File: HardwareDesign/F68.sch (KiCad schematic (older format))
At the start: 2 parts, among them J001 Conn_02x40_Counter_Clockwise

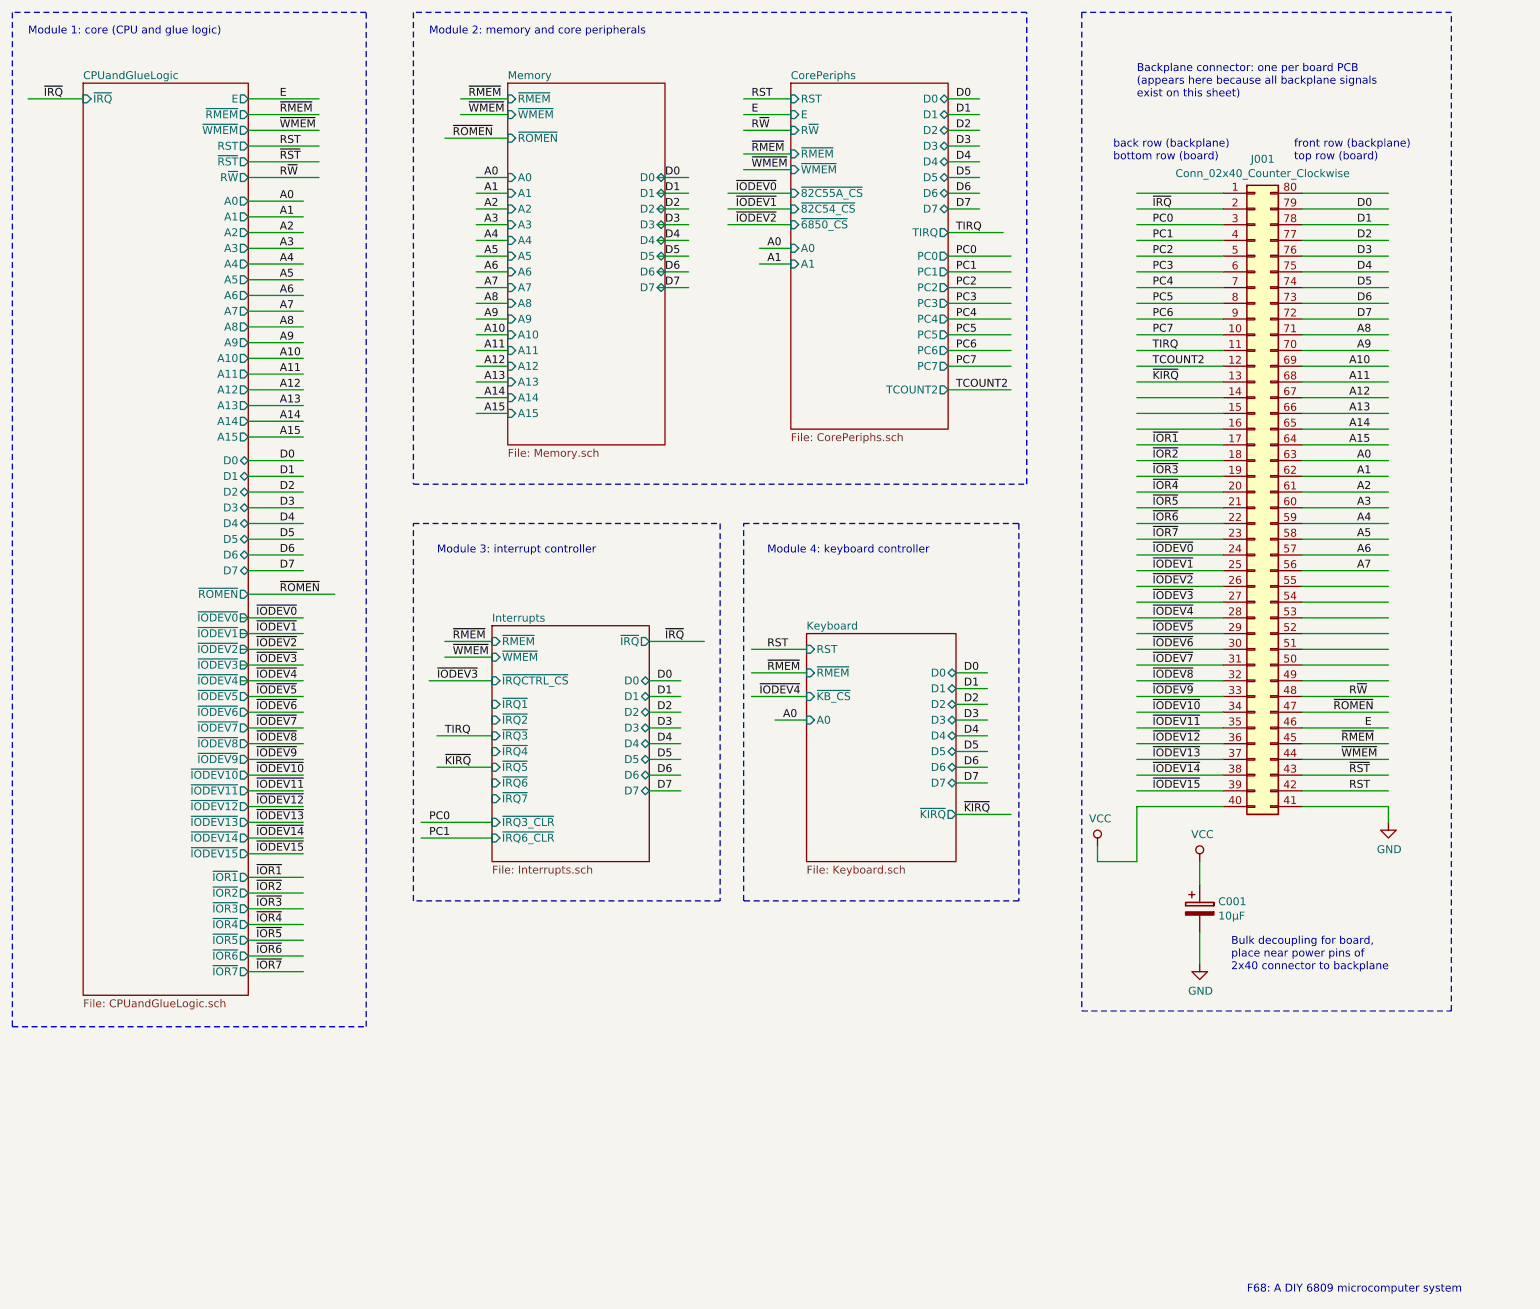
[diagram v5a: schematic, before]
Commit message: changes to backplane signals
Route all IRQ signals on backplane.

Only route -IOR1..-IOR3 on backplane.

Move TCOUNT2 to after IRQ signals.
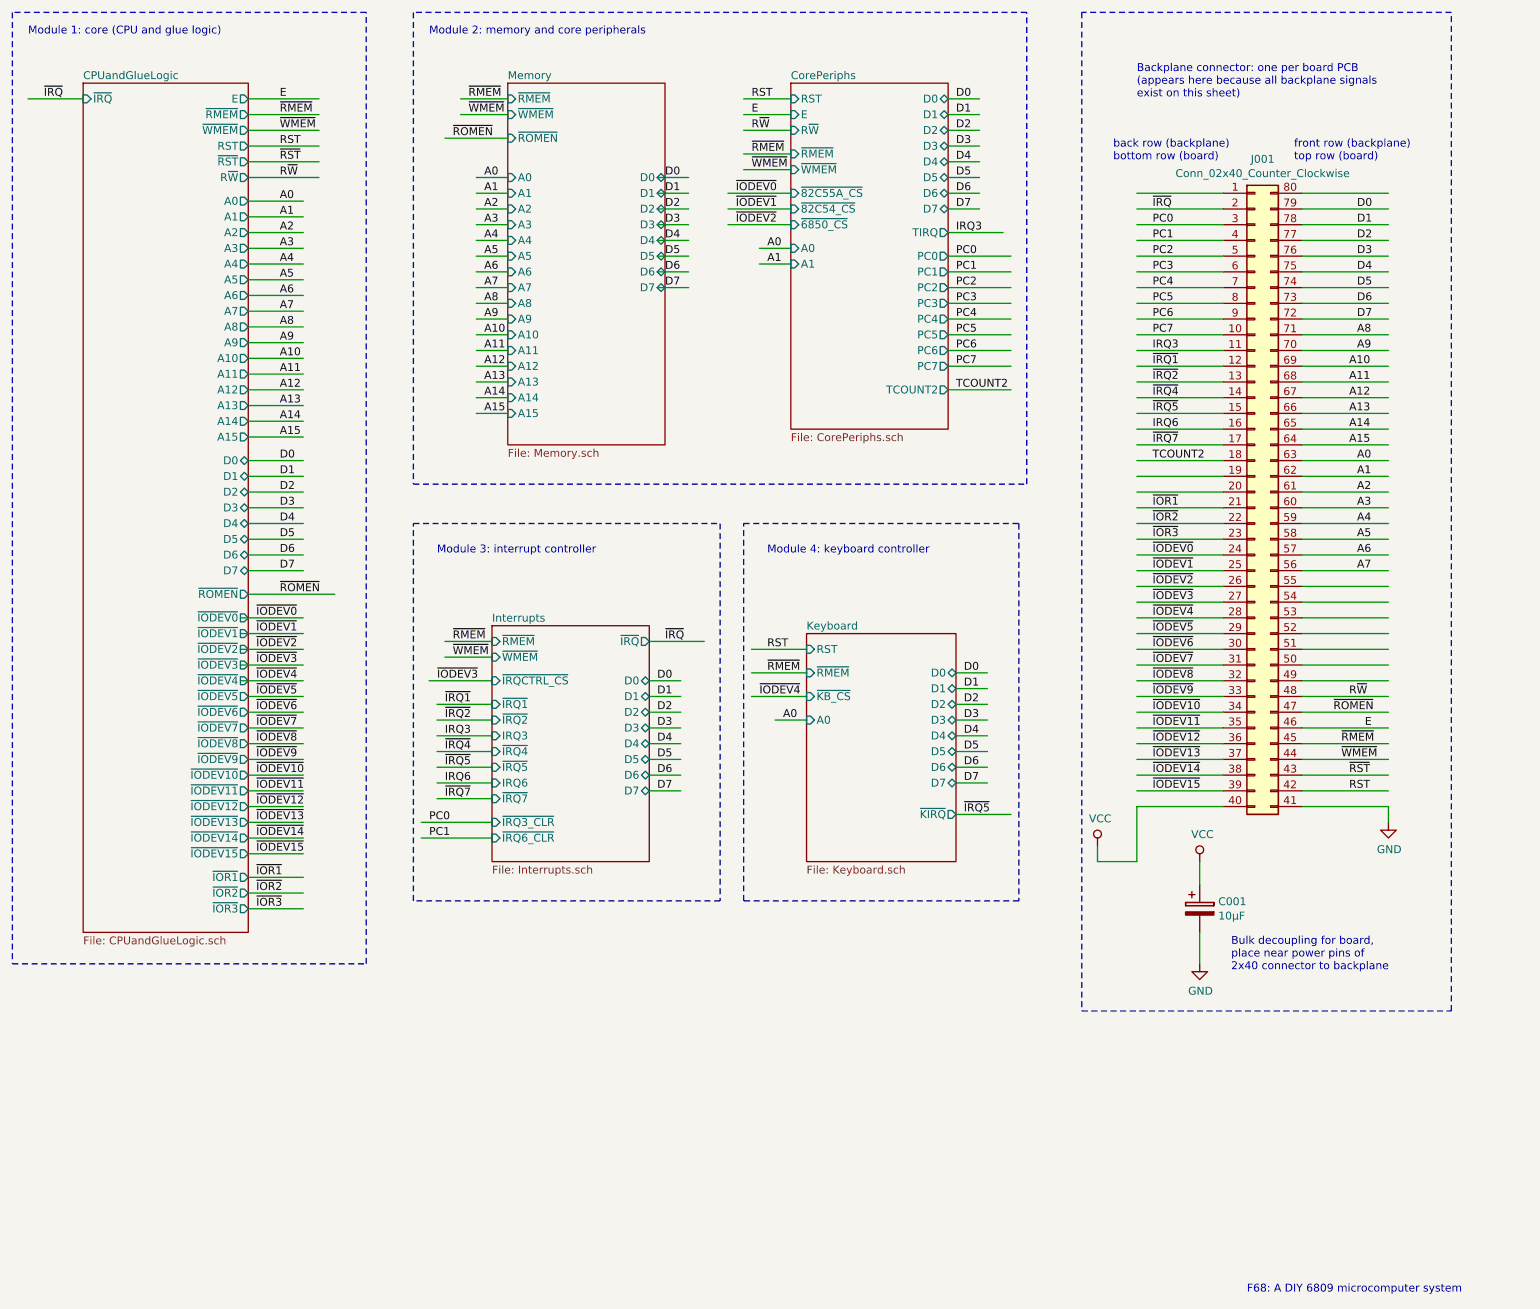
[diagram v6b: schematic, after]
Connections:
- net labels added: IRQ3, IRQ6, ~IRQ1~, ~IRQ2~, ~IRQ4~, ~IRQ5~, ~IRQ7~
- net labels removed: TIRQ, ~IOR4~, ~IOR5~, ~IOR6~, ~IOR7~, ~KIRQ~
- wire segments 225 -> 226
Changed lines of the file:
@@
 F68: A DIY 6809 microcomputer system
 $Sheet
-S 2200 1700 1050 5800
+S 2200 1700 1050 5400
 U 5CFA6AAA
 F0 "CPUandGlueLogic" 50
@@
 F51 "~IOR2~" O R 3250 6850 50
 F52 "~IOR3~" O R 3250 6950 50
-F53 "~IOR4~" O R 3250 7050 50
-F54 "~IOR5~" O R 3250 7150 50
-F55 "~IOR6~" O R 3250 7250 50
-F56 "~IOR7~" O R 3250 7350 50
 $EndSheet
 $Sheet
@@
 ~IODEV2
 Wire Notes Line
-	1750 1250 1750 7700
-Wire Notes Line
-	1750 7700 4000 7700
-Wire Notes Line
-	4000 7700 4000 1250
+	1750 1250 1750 7300
+Wire Notes Line
+	1750 7300 4000 7300
+Wire Notes Line
+	4000 7300 4000 1250
 Wire Notes Line
 	4000 1250 1750 1250
@@
 F5 "~IRQ5" I L 4800 6050 50
 F6 "~IRQ7" I L 4800 6250 50
-F7 "~IRQ3" I L 4800 5850 50
-F8 "~IRQ6" I L 4800 6150 50
-F9 "~IRQ" O R 5800 5250 50
-F10 "~RMEM" I L 4800 5250 50
-F11 "~IRQCTRL_CS" I L 4800 5500 50
-F12 "~IRQ3_CLR" I L 4800 6400 50
-F13 "~IRQ6_CLR" I L 4800 6500 50
-F14 "D0" B R 5800 5500 50
-F15 "D1" B R 5800 5600 50
-F16 "D2" B R 5800 5700 50
-F17 "D3" B R 5800 5800 50
-F18 "D4" B R 5800 5900 50
-F19 "D5" B R 5800 6000 50
-F20 "D6" B R 5800 6100 50
-F21 "D7" B R 5800 6200 50
-F22 "~WMEM" I L 4800 5350 50
+F7 "~IRQ" O R 5800 5250 50
+F8 "~RMEM" I L 4800 5250 50
+F9 "~IRQCTRL_CS" I L 4800 5500 50
+F10 "~IRQ3_CLR" I L 4800 6400 50
+F11 "~IRQ6_CLR" I L 4800 6500 50
+F12 "D0" B R 5800 5500 50
+F13 "D1" B R 5800 5600 50
+F14 "D2" B R 5800 5700 50
+F15 "D3" B R 5800 5800 50
+F16 "D4" B R 5800 5900 50
+F17 "D5" B R 5800 6000 50
+F18 "D6" B R 5800 6100 50
+F19 "D7" B R 5800 6200 50
+F20 "~WMEM" I L 4800 5350 50
+F21 "IRQ3" I L 4800 5850 50
+F22 "IRQ6" I L 4800 6150 50
 $EndSheet
 Wire Notes Line
@@
 	7700 2650 8050 2650
 Text Label 7750 2650 0    50   ~ 0
-TIRQ
+IRQ3
 Wire Wire Line
 	4450 5850 4800 5850
 Text Label 4500 5850 0    50   ~ 0
-TIRQ
+IRQ3
 Wire Wire Line
 	7700 2800 8100 2800
@@
 	7750 6350 8100 6350
 Text Label 7800 6350 0    50   ~ 0
-~KIRQ~
+~IRQ5~
 Wire Wire Line
 	4450 6050 4800 6050
 Text Label 4500 6050 0    50   ~ 0
-~KIRQ~
+~IRQ5~
 Wire Wire Line
 	7700 3650 8100 3650
@@
 	8900 3900 9450 3900
 Wire Wire Line
+	9950 4900 10500 4900
+Wire Wire Line
+	9950 5000 10500 5000
+Wire Wire Line
+	9950 5100 10500 5100
+Wire Wire Line
+	9950 5200 10500 5200
+Wire Wire Line
+	9950 5300 10500 5300
+Wire Wire Line
+	9950 5400 10500 5400
+Wire Wire Line
+	9950 5500 10500 5500
+Wire Wire Line
+	8900 4700 9450 4700
+Wire Wire Line
+	8900 4800 9450 4800
+Wire Wire Line
+	8900 4900 9450 4900
+Wire Wire Line
+	8900 5000 9450 5000
+Wire Wire Line
+	8900 5100 9450 5100
+Wire Wire Line
+	8900 5200 9450 5200
+Wire Wire Line
+	8900 5300 9450 5300
+Wire Wire Line
+	8900 5400 9450 5400
+Wire Wire Line
+	8900 5500 9450 5500
+Wire Wire Line
+	8900 5600 9450 5600
+Wire Wire Line
+	8900 5700 9450 5700
+Wire Wire Line
+	8900 5800 9450 5800
+Wire Wire Line
+	8900 5900 9450 5900
+Wire Wire Line
+	8900 6000 9450 6000
+Wire Wire Line
+	8900 6100 9450 6100
+Wire Wire Line
+	8900 6200 9450 6200
+Wire Wire Line
+	8900 6300 9450 6300
+Wire Wire Line
+	9950 2400 10500 2400
+Wire Wire Line
+	9950 2500 10500 2500
+Wire Wire Line
+	9950 2600 10500 2600
+Wire Wire Line
+	9950 2700 10500 2700
+Wire Wire Line
+	9950 2800 10500 2800
+Wire Wire Line
+	9950 2900 10500 2900
+Wire Wire Line
+	9950 3000 10500 3000
+Wire Wire Line
+	9950 3100 10500 3100
+Wire Wire Line
+	9950 3200 10500 3200
+Wire Wire Line
+	9950 3300 10500 3300
+Wire Wire Line
+	9950 3400 10500 3400
+Wire Wire Line
+	9950 3500 10500 3500
+Wire Wire Line
+	9950 3600 10500 3600
+Wire Wire Line
+	9950 3700 10500 3700
+Wire Wire Line
+	9950 3800 10500 3800
+Wire Wire Line
+	9950 3900 10500 3900
+Wire Wire Line
+	9950 4000 10500 4000
+Wire Wire Line
+	9950 4100 10500 4100
+Wire Wire Line
+	9950 4200 10500 4200
+Wire Wire Line
+	9950 4300 10500 4300
+Wire Wire Line
+	9950 4400 10500 4400
+Wire Wire Line
+	9950 4500 10500 4500
+Wire Wire Line
+	9950 4600 10500 4600
+Wire Wire Line
+	9950 4700 10500 4700
+Wire Wire Line
+	9950 4800 10500 4800
+Wire Wire Line
 	8900 4000 9450 4000
 Wire Wire Line
@@
 Wire Wire Line
 	8900 4600 9450 4600
-Wire Wire Line
-	8900 4700 9450 4700
-Wire Wire Line
-	8900 4800 9450 4800
-Wire Wire Line
-	8900 4900 9450 4900
-Wire Wire Line
-	8900 5000 9450 5000
-Wire Wire Line
-	8900 5100 9450 5100
-Wire Wire Line
-	8900 5200 9450 5200
-Wire Wire Line
-	8900 5300 9450 5300
-Wire Wire Line
-	8900 5400 9450 5400
-Wire Wire Line
-	8900 5500 9450 5500
-Wire Wire Line
-	8900 5600 9450 5600
-Wire Wire Line
-	8900 5700 9450 5700
-Wire Wire Line
-	8900 5800 9450 5800
-Wire Wire Line
-	8900 5900 9450 5900
-Wire Wire Line
-	8900 6000 9450 6000
-Wire Wire Line
-	8900 6100 9450 6100
-Wire Wire Line
-	8900 6200 9450 6200
-Wire Wire Line
-	8900 6300 9450 6300
-Wire Wire Line
-	9950 2400 10500 2400
-Wire Wire Line
-	9950 2500 10500 2500
-Wire Wire Line
-	9950 2600 10500 2600
-Wire Wire Line
-	9950 2700 10500 2700
-Wire Wire Line
-	9950 2800 10500 2800
-Wire Wire Line
-	9950 2900 10500 2900
-Wire Wire Line
-	9950 3000 10500 3000
-Wire Wire Line
-	9950 3100 10500 3100
-Wire Wire Line
-	9950 3200 10500 3200
-Wire Wire Line
-	9950 3300 10500 3300
-Wire Wire Line
-	9950 3400 10500 3400
-Wire Wire Line
-	9950 3500 10500 3500
-Wire Wire Line
-	9950 3600 10500 3600
-Wire Wire Line
-	9950 3700 10500 3700
-Wire Wire Line
-	9950 3800 10500 3800
-Wire Wire Line
-	9950 3900 10500 3900
-Wire Wire Line
-	9950 4000 10500 4000
-Wire Wire Line
-	9950 4100 10500 4100
-Wire Wire Line
-	9950 4200 10500 4200
-Wire Wire Line
-	9950 4300 10500 4300
-Wire Wire Line
-	9950 4400 10500 4400
-Wire Wire Line
-	9950 4500 10500 4500
-Wire Wire Line
-	9950 4600 10500 4600
-Wire Wire Line
-	9950 4700 10500 4700
-Wire Wire Line
-	9950 4800 10500 4800
-Wire Wire Line
-	9950 4900 10500 4900
-Wire Wire Line
-	9950 5000 10500 5000
-Wire Wire Line
-	9950 5100 10500 5100
-Wire Wire Line
-	9950 5200 10500 5200
-Wire Wire Line
-	9950 5300 10500 5300
-Wire Wire Line
-	9950 5400 10500 5400
-Wire Wire Line
-	9950 5500 10500 5500
 Wire Wire Line
 	9950 5600 10500 5600
@@
 PC7
 Text Label 9000 3400 0    50   ~ 0
-TIRQ
+IRQ3
 Wire Wire Line
 	8650 6650 8650 6550
@@
 Text Notes 9900 2200 0    50   ~ 0
 front row (backplane)\ntop row (board)
-Text Label 9000 4000 0    50   ~ 0
+Text Label 9000 4400 0    50   ~ 0
 ~IOR1~
+Text Label 9000 4500 0    50   ~ 0
+~IOR2~
+Text Label 9000 4600 0    50   ~ 0
+~IOR3~
 Text Label 9000 4100 0    50   ~ 0
-~IOR2~
-Text Label 9000 4200 0    50   ~ 0
-~IOR3~
-Text Label 9000 4300 0    50   ~ 0
-~IOR4~
-Text Label 9000 4400 0    50   ~ 0
-~IOR5~
-Text Label 9000 4500 0    50   ~ 0
-~IOR6~
-Text Label 9000 4600 0    50   ~ 0
-~IOR7~
-Text Label 9000 3500 0    50   ~ 0
 TCOUNT2
 Text Notes 8900 1800 0    50   ~ 0
@@
 Wire Wire Line
 	3250 6950 3600 6950
-Wire Wire Line
-	3250 7050 3600 7050
-Wire Wire Line
-	3250 7150 3600 7150
-Wire Wire Line
-	3250 7250 3600 7250
-Wire Wire Line
-	3250 7350 3600 7350
 Text Label 3300 6750 0    50   ~ 0
 ~IOR1~
@@
 Text Label 3300 6950 0    50   ~ 0
 ~IOR3~
-Text Label 3300 7050 0    50   ~ 0
-~IOR4~
-Text Label 3300 7150 0    50   ~ 0
-~IOR5~
-Text Label 3300 7250 0    50   ~ 0
-~IOR6~
-Text Label 3300 7350 0    50   ~ 0
-~IOR7~
-Text Label 9000 3600 0    50   ~ 0
-~KIRQ~
 Wire Notes Line
 	8550 1250 8550 7600
@@
 Text Notes 9500 7350 0    50   ~ 0
 Bulk decoupling for board,\nplace near power pins of\n2x40 connector to backplane
+Text Label 9000 3800 0    50   ~ 0
+~IRQ5~
+Text Label 9000 3500 0    50   ~ 0
+~IRQ1~
+Text Label 9000 3600 0    50   ~ 0
+~IRQ2~
+Text Label 9000 3700 0    50   ~ 0
+~IRQ4~
+Text Label 9000 3900 0    50   ~ 0
+IRQ6
+Text Label 9000 4000 0    50   ~ 0
+~IRQ7~
+Wire Wire Line
+	4450 5650 4800 5650
+Wire Wire Line
+	4450 5750 4800 5750
+Text Label 4500 5650 0    50   ~ 0
+~IRQ1~
+Text Label 4500 5750 0    50   ~ 0
+~IRQ2~
+Wire Wire Line
+	4450 5950 4800 5950
+Text Label 4500 5950 0    50   ~ 0
+~IRQ4~
+Wire Wire Line
+	4450 6150 4800 6150
+Wire Wire Line
+	4450 6250 4800 6250
+Text Label 4500 6150 0    50   ~ 0
+IRQ6
+Text Label 4500 6250 0    50   ~ 0
+~IRQ7~
 $EndSCHEMATC

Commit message: assigned component footprints
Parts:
- C001: footprint (none) -> Capacitor_THT:CP_Radial_D6.3mm_P2.50mm
- J001: footprint (none) -> Connector_PinHeader_2.54mm:PinHeader_2x40_P2.54mm_Vertical
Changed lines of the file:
@@
 F 0 "J001" H 9700 6417 50  0000 C CNN
 F 1 "Conn_02x40_Counter_Clockwise" H 9700 6326 50  0000 C CNN
-F 2 "" H 9650 4300 50  0001 C CNN
+F 2 "Connector_PinHeader_2.54mm:PinHeader_2x40_P2.54mm_Vertical" H 9650 4300 50  0001 C CNN
 F 3 "~" H 9650 4300 50  0001 C CNN
 	1    9650 4300
@@
 AR Path="/5CFA6AAA/611835E5" Ref="#PWR?"  Part="1"
 AR Path="/5D49B078/611835E5" Ref="#PWR?"  Part="1"
-AR Path="/611835E5" Ref="#PWR?"  Part="1"
-F 0 "#PWR?" H 10500 6150 50  0001 C CNN
+AR Path="/611835E5" Ref="#PWR0105"  Part="1"
+F 0 "#PWR0105" H 10500 6150 50  0001 C CNN
 F 1 "GND" H 10505 6227 50  0000 C CNN
 F 2 "" H 10500 6400 50  0001 C CNN
@@
 P 8650 6550
 AR Path="/5D49B078/61183609" Ref="#PWR?"  Part="1"
-AR Path="/61183609" Ref="#PWR?"  Part="1"
-F 0 "#PWR?" H 8650 6400 50  0001 C CNN
+AR Path="/61183609" Ref="#PWR0131"  Part="1"
+F 0 "#PWR0131" H 8650 6400 50  0001 C CNN
 F 1 "VCC" H 8667 6723 50  0000 C CNN
 F 2 "" H 8650 6550 50  0001 C CNN
@@
 F 0 "C001" H 9418 6996 50  0000 L CNN
 F 1 "10μF" H 9418 6905 50  0000 L CNN
-F 2 "" H 9338 6800 50  0001 C CNN
+F 2 "Capacitor_THT:CP_Radial_D6.3mm_P2.50mm" H 9338 6800 50  0001 C CNN
 F 3 "" H 9300 6950 50  0001 C CNN
 	1    9300 6950
@@
 P 9300 6650
 AR Path="/5CFA6AAA/619F2ED5" Ref="#PWR?"  Part="1"
-AR Path="/619F2ED5" Ref="#PWR?"  Part="1"
-F 0 "#PWR?" H 9300 6500 50  0001 C CNN
+AR Path="/619F2ED5" Ref="#PWR0132"  Part="1"
+F 0 "#PWR0132" H 9300 6500 50  0001 C CNN
 F 1 "VCC" H 9317 6823 50  0000 C CNN
 F 2 "" H 9300 6650 50  0001 C CNN
@@
 P 9300 7300
 AR Path="/5CFA6AAA/619F2EDC" Ref="#PWR?"  Part="1"
-AR Path="/619F2EDC" Ref="#PWR?"  Part="1"
-F 0 "#PWR?" H 9300 7050 50  0001 C CNN
+AR Path="/619F2EDC" Ref="#PWR0133"  Part="1"
+F 0 "#PWR0133" H 9300 7050 50  0001 C CNN
 F 1 "GND" H 9305 7127 50  0000 C CNN
 F 2 "" H 9300 7300 50  0001 C CNN
